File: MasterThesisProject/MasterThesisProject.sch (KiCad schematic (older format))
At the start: 42 parts

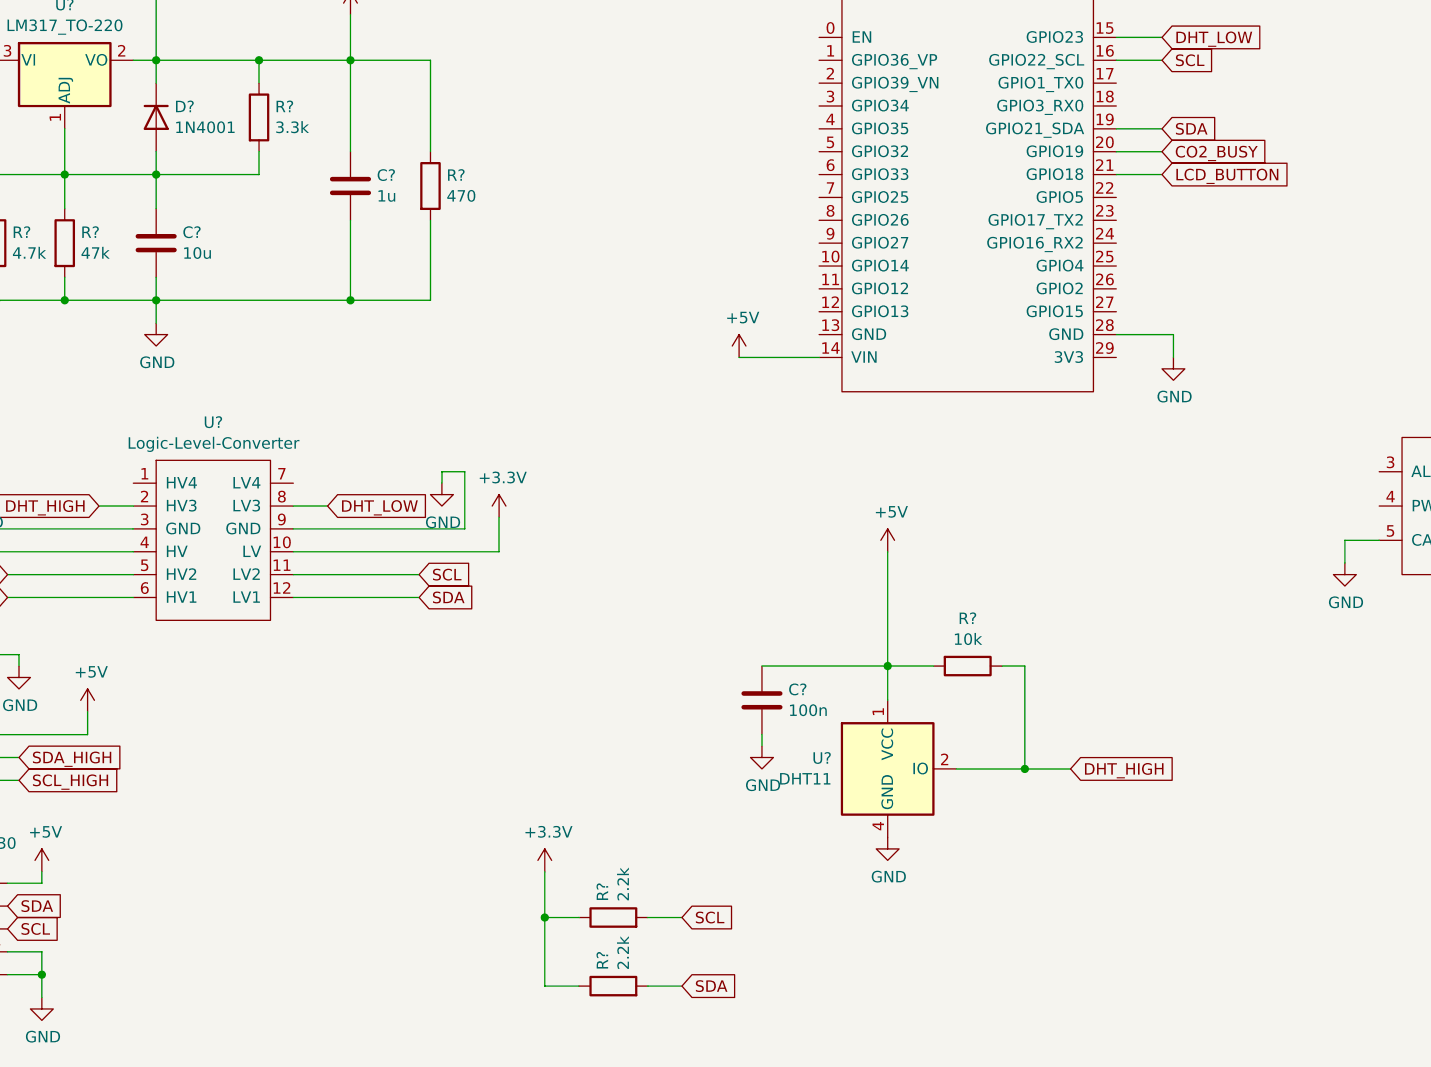
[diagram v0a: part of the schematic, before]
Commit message: Add spi_eth and co_sensor connections to schematic
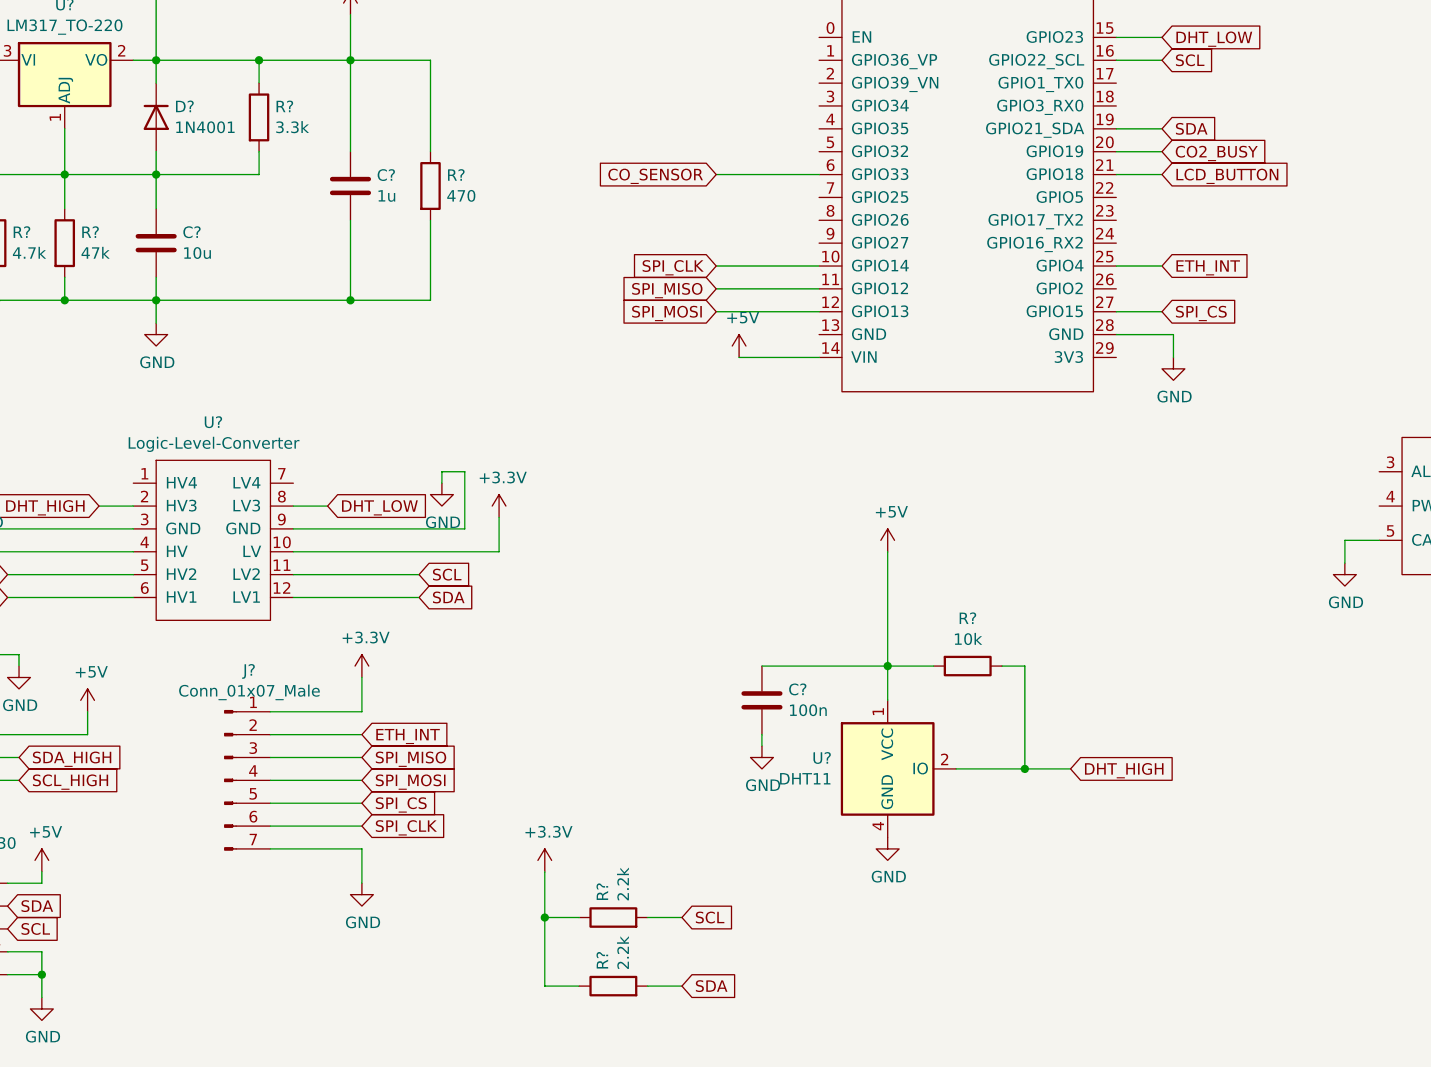
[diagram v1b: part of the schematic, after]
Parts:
- added J?: Conn_01x07_Male, symbol Connector:Conn_01x07_Male
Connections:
- net +3V3: now also J?.1 (Pin_1)
- net CO_SENSOR: now also U?.6 (GPIO33)
- net GND: now also J?.7 (Pin_7)
- net SPI_CLK: now reaches U?.10 (GPIO14)
- net SPI_CLK: now also J?.6 (Pin_6)
- net SPI_MISO: now reaches U?.11 (GPIO12)
- net SPI_MISO: now also J?.3 (Pin_3)
- net SPI_MOSI: now reaches U?.12 (GPIO13)
- net SPI_MOSI: now also J?.4 (Pin_4)
- net ETH_INT: now reaches U?.25 (GPIO4)
- net ETH_INT: now also J?.2 (Pin_2)
- net SPI_CS: now reaches U?.27 (GPIO15)
- net SPI_CS: now also J?.5 (Pin_5)
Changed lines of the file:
@@
 Wire Wire Line
 	1800 4550 1800 4450
+$Comp
+L Connector:Conn_01x07_Male J?
+U 1 1 608ED61E
+P 2100 6550
+F 0 "J?" H 2208 7031 50  0000 C CNN
+F 1 "Conn_01x07_Male" H 2208 6940 50  0000 C CNN
+F 2 "" H 2100 6550 50  0001 C CNN
+F 3 "~" H 2100 6550 50  0001 C CNN
+	1    2100 6550
+	1    0    0    -1
+$EndComp
+Text GLabel 4250 4500 0    50   Input ~ 0
+SPI_MOSI
+Text GLabel 4250 4400 0    50   Input ~ 0
+SPI_MISO
+Text GLabel 4250 4300 0    50   Input ~ 0
+SPI_CLK
+Text GLabel 6200 4500 2    50   Input ~ 0
+SPI_CS
+Wire Wire Line
+	4700 4300 4250 4300
+Wire Wire Line
+	4250 4400 4700 4400
+Wire Wire Line
+	4700 4500 4250 4500
+Wire Wire Line
+	6200 4500 6000 4500
+Text GLabel 6200 4300 2    50   Input ~ 0
+ETH_INT
+Wire Wire Line
+	6200 4300 6000 4300
+Wire Wire Line
+	2300 6250 2700 6250
+Wire Wire Line
+	2700 6250 2700 6100
+Wire Wire Line
+	2300 6850 2700 6850
+Wire Wire Line
+	2700 6850 2700 7000
+$Comp
+L power:GND #PWR?
+U 1 1 6095011A
+P 2700 7000
+F 0 "#PWR?" H 2700 6750 50  0001 C CNN
+F 1 "GND" H 2705 6827 50  0000 C CNN
+F 2 "" H 2700 7000 50  0001 C CNN
+F 3 "" H 2700 7000 50  0001 C CNN
+	1    2700 7000
+	1    0    0    -1
+$EndComp
+$Comp
+L power:+3.3V #PWR?
+U 1 1 60950EB2
+P 2700 6100
+F 0 "#PWR?" H 2700 5950 50  0001 C CNN
+F 1 "+3.3V" H 2715 6273 50  0000 C CNN
+F 2 "" H 2700 6100 50  0001 C CNN
+F 3 "" H 2700 6100 50  0001 C CNN
+	1    2700 6100
+	1    0    0    -1
+$EndComp
+Text GLabel 2700 6350 2    50   Input ~ 0
+ETH_INT
+Text GLabel 2700 6450 2    50   Input ~ 0
+SPI_MISO
+Text GLabel 2700 6550 2    50   Input ~ 0
+SPI_MOSI
+Text GLabel 2700 6650 2    50   Input ~ 0
+SPI_CS
+Text GLabel 2700 6750 2    50   Input ~ 0
+SPI_CLK
+Wire Wire Line
+	2700 6350 2300 6350
+Wire Wire Line
+	2300 6450 2700 6450
+Wire Wire Line
+	2700 6550 2300 6550
+Wire Wire Line
+	2300 6650 2700 6650
+Wire Wire Line
+	2700 6750 2300 6750
+Wire Wire Line
+	4700 3900 4250 3900
+Text GLabel 4250 3900 0    50   Input ~ 0
+CO_SENSOR
 $EndSCHEMATC

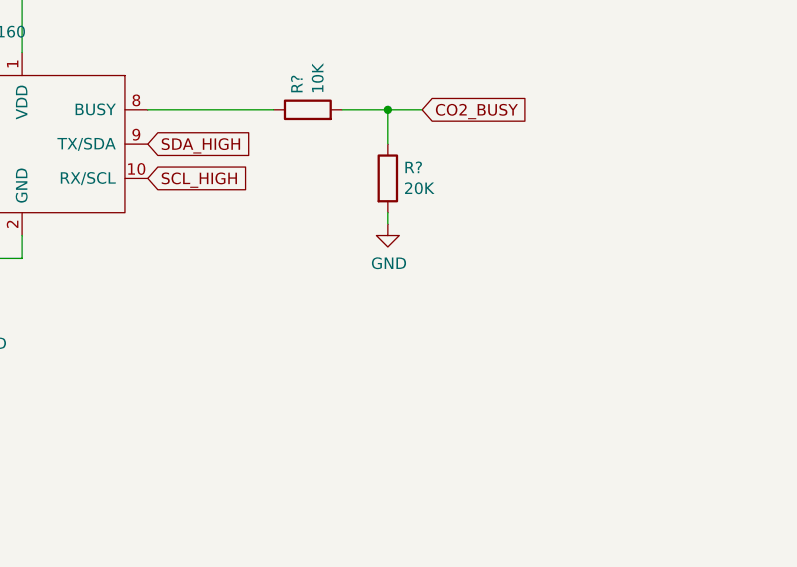
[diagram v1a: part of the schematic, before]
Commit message: Add footprints to resistors
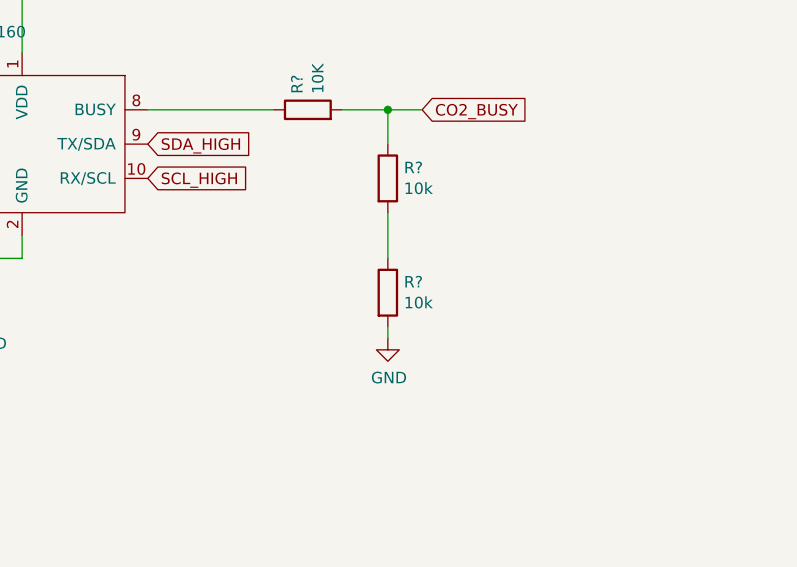
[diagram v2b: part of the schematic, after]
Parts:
- added R?: 10k, Resistor_SMD:R_0805_2012Metric_Pad1.20x1.40mm_HandSolder, symbol Device:R
- R? (x16): footprint (none) -> Resistor_SMD:R_0805_2012Metric_Pad1.20x1.40mm_HandSolder
- R?: value 20K -> 10k; footprint (none) -> Resistor_SMD:R_0805_2012Metric_Pad1.20x1.40mm_HandSolder
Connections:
- net CO2_BUSY: now also R?.1; no longer R?.1
- new net: R?.1, R?.2
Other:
- moved on the sheet: R?
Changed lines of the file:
@@
 F 0 "R?" H 3870 7196 50  0000 L CNN
 F 1 "2.2k" H 3870 7105 50  0000 L CNN
-F 2 "" V 3730 7150 50  0001 C CNN
+F 2 "Resistor_SMD:R_0805_2012Metric_Pad1.20x1.40mm_HandSolder" V 3730 7150 50  0001 C CNN
 F 3 "~" H 3800 7150 50  0001 C CNN
 	1    3800 7150
@@
 F 0 "R?" H 3870 7496 50  0000 L CNN
 F 1 "2.2k" H 3870 7405 50  0000 L CNN
-F 2 "" V 3730 7450 50  0001 C CNN
+F 2 "Resistor_SMD:R_0805_2012Metric_Pad1.20x1.40mm_HandSolder" V 3730 7450 50  0001 C CNN
 F 3 "~" H 3800 7450 50  0001 C CNN
 	1    3800 7450
@@
 F 0 "R?" H 3620 1196 50  0000 L CNN
 F 1 "10k" H 3620 1105 50  0000 L CNN
-F 2 "" V 3480 1150 50  0001 C CNN
+F 2 "Resistor_SMD:R_0805_2012Metric_Pad1.20x1.40mm_HandSolder" V 3480 1150 50  0001 C CNN
 F 3 "~" H 3550 1150 50  0001 C CNN
 	1    3550 1150
@@
 F 0 "R?" H 4020 1546 50  0000 L CNN
 F 1 "10k" H 4020 1455 50  0000 L CNN
-F 2 "" V 3880 1500 50  0001 C CNN
+F 2 "Resistor_SMD:R_0805_2012Metric_Pad1.20x1.40mm_HandSolder" V 3880 1500 50  0001 C CNN
 F 3 "~" H 3950 1500 50  0001 C CNN
 	1    3950 1500
@@
 F 0 "R?" H 6870 1796 50  0000 L CNN
 F 1 "1k" H 6870 1705 50  0000 L CNN
-F 2 "" V 6730 1750 50  0001 C CNN
+F 2 "Resistor_SMD:R_0805_2012Metric_Pad1.20x1.40mm_HandSolder" V 6730 1750 50  0001 C CNN
 F 3 "~" H 6800 1750 50  0001 C CNN
 	1    6800 1750
@@
 F 0 "R?" H 6870 2296 50  0000 L CNN
 F 1 "1k" H 6870 2205 50  0000 L CNN
-F 2 "" V 6730 2250 50  0001 C CNN
+F 2 "Resistor_SMD:R_0805_2012Metric_Pad1.20x1.40mm_HandSolder" V 6730 2250 50  0001 C CNN
 F 3 "~" H 6800 2250 50  0001 C CNN
 	1    6800 2250
@@
 F 0 "R?" H 8770 2246 50  0000 L CNN
 F 1 "1k" H 8770 2155 50  0000 L CNN
-F 2 "" V 8630 2200 50  0001 C CNN
+F 2 "Resistor_SMD:R_0805_2012Metric_Pad1.20x1.40mm_HandSolder" V 8630 2200 50  0001 C CNN
 F 3 "~" H 8700 2200 50  0001 C CNN
 	1    8700 2200
@@
 F 0 "R?" H 9320 5246 50  0000 L CNN
 F 1 "10K" H 9320 5155 50  0000 L CNN
-F 2 "" V 9180 5200 50  0001 C CNN
+F 2 "Resistor_SMD:R_0805_2012Metric_Pad1.20x1.40mm_HandSolder" V 9180 5200 50  0001 C CNN
 F 3 "~" H 9250 5200 50  0001 C CNN
 	1    9250 5200
@@
 L Device:R R?
 U 1 1 6059A344
-P 9600 5500
-F 0 "R?" H 9670 5546 50  0000 L CNN
-F 1 "20K" H 9670 5455 50  0000 L CNN
-F 2 "" V 9530 5500 50  0001 C CNN
-F 3 "~" H 9600 5500 50  0001 C CNN
-	1    9600 5500
+P 9600 6000
+F 0 "R?" H 9670 6046 50  0000 L CNN
+F 1 "10k" H 9670 5955 50  0000 L CNN
+F 2 "Resistor_SMD:R_0805_2012Metric_Pad1.20x1.40mm_HandSolder" V 9530 6000 50  0001 C CNN
+F 3 "~" H 9600 6000 50  0001 C CNN
+	1    9600 6000
 	1    0    0    -1
 $EndComp
@@
 	9600 5200 9600 5350
 Wire Wire Line
-	9600 5650 9600 5700
+	9600 6150 9600 6200
 Wire Wire Line
 	9600 5200 9750 5200
@@
 L power:GND #PWR?
 U 1 1 60574544
-P 9600 5700
-F 0 "#PWR?" H 9600 5450 50  0001 C CNN
-F 1 "GND" H 9605 5527 50  0000 C CNN
-F 2 "" H 9600 5700 50  0001 C CNN
-F 3 "" H 9600 5700 50  0001 C CNN
-	1    9600 5700
+P 9600 6200
+F 0 "#PWR?" H 9600 5950 50  0001 C CNN
+F 1 "GND" H 9605 6027 50  0000 C CNN
+F 2 "" H 9600 6200 50  0001 C CNN
+F 3 "" H 9600 6200 50  0001 C CNN
+	1    9600 6200
 	1    0    0    -1
 $EndComp
@@
 F 0 "R?" H 8409 1446 50  0000 L CNN
 F 1 "68" H 8409 1355 50  0000 L CNN
-F 2 "" H 8350 1400 50  0001 C CNN
+F 2 "Resistor_SMD:R_0805_2012Metric_Pad1.20x1.40mm_HandSolder" H 8350 1400 50  0001 C CNN
 F 3 "~" H 8350 1400 50  0001 C CNN
 	1    8350 1400
@@
 F 0 "R?" H 7670 1496 50  0000 L CNN
 F 1 "330" H 7670 1405 50  0000 L CNN
-F 2 "" V 7530 1450 50  0001 C CNN
+F 2 "Resistor_SMD:R_0805_2012Metric_Pad1.20x1.40mm_HandSolder" V 7530 1450 50  0001 C CNN
 F 3 "~" H 7600 1450 50  0001 C CNN
 	1    7600 1450
@@
 F 0 "R?" V 9643 1400 50  0000 C CNN
 F 1 "470" V 9734 1400 50  0000 C CNN
-F 2 "" V 9780 1400 50  0001 C CNN
+F 2 "Resistor_SMD:R_0805_2012Metric_Pad1.20x1.40mm_HandSolder" V 9780 1400 50  0001 C CNN
 F 3 "~" H 9850 1400 50  0001 C CNN
 	1    9850 1400
@@
 F 0 "R?" V 5143 6050 50  0000 C CNN
 F 1 "10k" V 5234 6050 50  0000 C CNN
-F 2 "" V 5280 6050 50  0001 C CNN
+F 2 "Resistor_SMD:R_0805_2012Metric_Pad1.20x1.40mm_HandSolder" V 5280 6050 50  0001 C CNN
 F 3 "~" H 5350 6050 50  0001 C CNN
 	1    5350 6050
@@
 F 0 "R?" H 2320 3696 50  0000 L CNN
 F 1 "3.3k" H 2320 3605 50  0000 L CNN
-F 2 "" V 2180 3650 50  0001 C CNN
+F 2 "Resistor_SMD:R_0805_2012Metric_Pad1.20x1.40mm_HandSolder" V 2180 3650 50  0001 C CNN
 F 3 "~" H 2250 3650 50  0001 C CNN
 	1    2250 3650
@@
 F 0 "R?" H 1470 4246 50  0000 L CNN
 F 1 "47k" H 1470 4155 50  0000 L CNN
-F 2 "" V 1330 4200 50  0001 C CNN
+F 2 "Resistor_SMD:R_0805_2012Metric_Pad1.20x1.40mm_HandSolder" V 1330 4200 50  0001 C CNN
 F 3 "~" H 1400 4200 50  0001 C CNN
 	1    1400 4200
@@
 F 0 "R?" H 1170 4246 50  0000 L CNN
 F 1 "4.7k" H 1170 4155 50  0000 L CNN
-F 2 "" V 1030 4200 50  0001 C CNN
+F 2 "Resistor_SMD:R_0805_2012Metric_Pad1.20x1.40mm_HandSolder" V 1030 4200 50  0001 C CNN
 F 3 "~" H 1100 4200 50  0001 C CNN
 	1    1100 4200
@@
 F 0 "R?" H 3070 3996 50  0000 L CNN
 F 1 "470" H 3070 3905 50  0000 L CNN
-F 2 "" V 2930 3950 50  0001 C CNN
+F 2 "Resistor_SMD:R_0805_2012Metric_Pad1.20x1.40mm_HandSolder" V 2930 3950 50  0001 C CNN
 F 3 "~" H 3000 3950 50  0001 C CNN
 	1    3000 3950
@@
 Text GLabel 4250 3900 0    50   Input ~ 0
 CO_SENSOR
+$Comp
+L Device:R R?
+U 1 1 609F478E
+P 9600 5500
+F 0 "R?" H 9670 5546 50  0000 L CNN
+F 1 "10k" H 9670 5455 50  0000 L CNN
+F 2 "Resistor_SMD:R_0805_2012Metric_Pad1.20x1.40mm_HandSolder" V 9530 5500 50  0001 C CNN
+F 3 "~" H 9600 5500 50  0001 C CNN
+	1    9600 5500
+	1    0    0    -1
+$EndComp
+Wire Wire Line
+	9600 5650 9600 5850
 $EndSCHEMATC
